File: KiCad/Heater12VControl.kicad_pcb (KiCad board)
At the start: 2 copper layers, 19.2 x 13.9 mm, 11 parts, among them J1 12V, J2 Arduino, J3 Heater, J4 Temp sensor, Q1 SI2308, Q2 IRLR3715

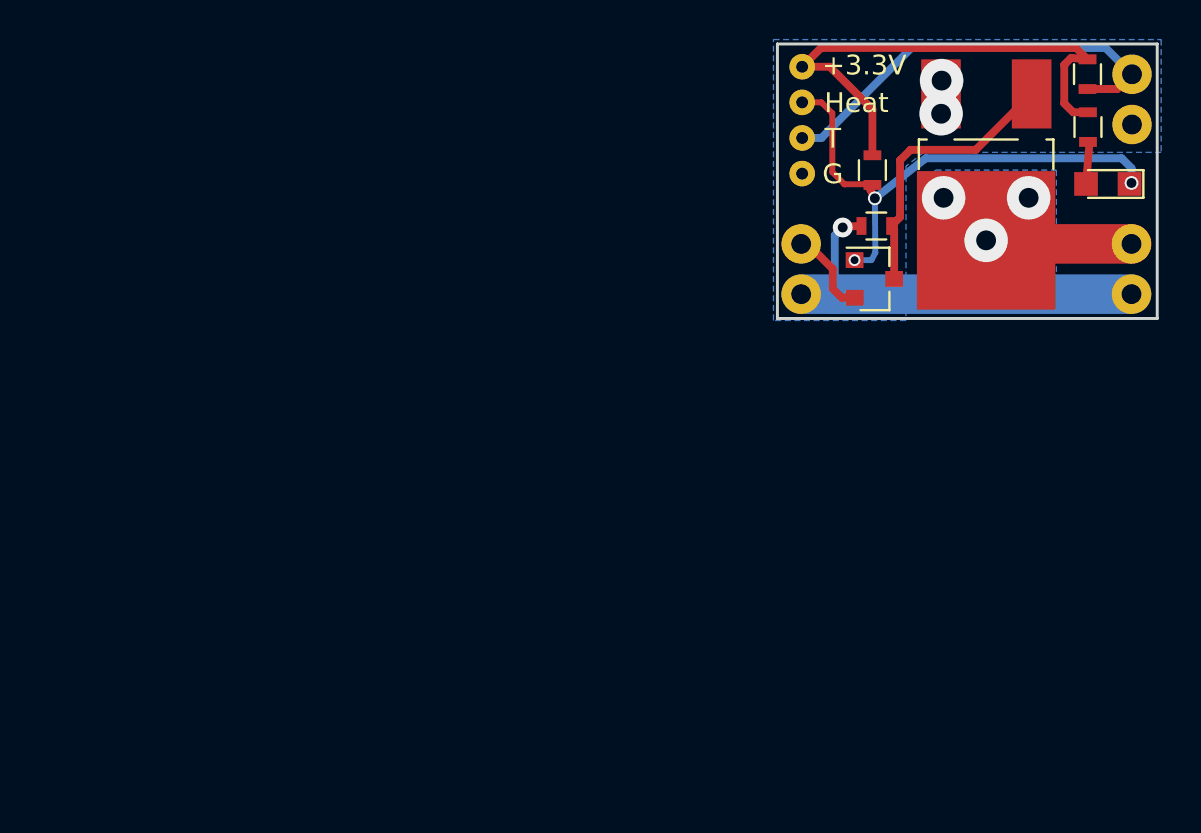
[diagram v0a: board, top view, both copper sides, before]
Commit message: New Version with rotary encoder and AIO pcb
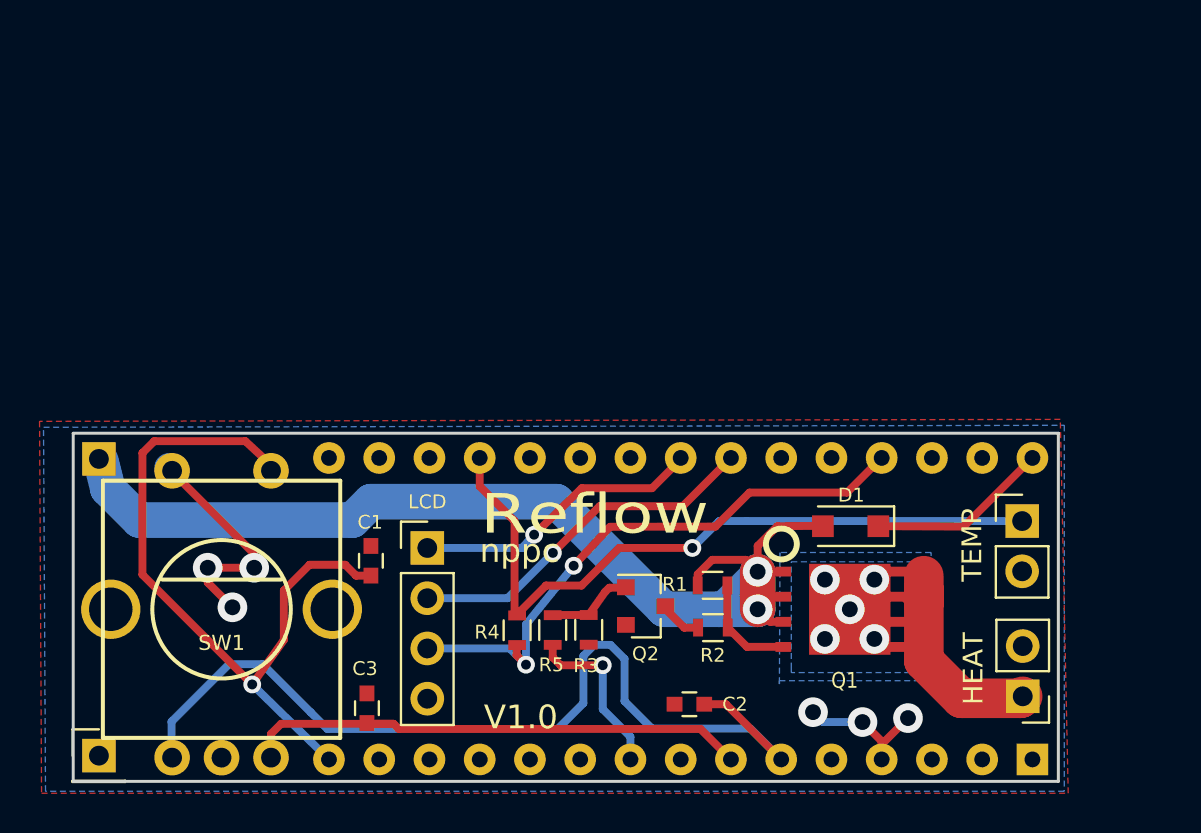
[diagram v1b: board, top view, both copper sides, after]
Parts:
- removed J1: 12V, KiCad_custom:Conn2pin_2.54mm
- removed J2: Arduino, KiCad_custom:conn_4pin_TH_1.8mm
- removed J3: Heater, KiCad_custom:Conn2pin_2.54mm
- added 12V: PWR, Pin_Headers:Pin_Header_Straight_1x01_Pitch2.54mm, F.Cu at (124.6, 119.8)
- added C1: 22n, Capacitors_SMD:C_0603, F.Cu at (138.3, 125.0)
- added C2: 22n, Capacitors_SMD:C_0603, F.Cu at (154.4, 132.2)
- added C3: 22n, Capacitors_SMD:C_0603, F.Cu at (138.2, 132.4)
- added GND: PWR, Pin_Headers:Pin_Header_Straight_1x01_Pitch2.54mm, F.Cu at (124.6, 134.8)
- added HEAT: Heater, Pin_Headers:Pin_Header_Straight_1x02_Pitch2.54mm, F.Cu at (171.3, 131.8)
- added LCD: LCD, Pin_Headers:Pin_Header_Straight_1x04_Pitch2.54mm, F.Cu at (141.2, 124.3)
- added R5: 100, Resistors_SMD:R_0603, F.Cu at (147.5, 128.4)
- added SW1: Rotary_Encoder, ROTARY-ENCODER, F.Cu at (130.8, 127.4)
- added TEMP: Temp sensor, Pin_Headers:Pin_Header_Straight_1x02_Pitch2.54mm, F.Cu at (171.3, 122.9)
- D1: value LED -> D; footprint LEDs:LED_0805 -> Diodes_SMD:D_SOD-123F
- J4: value Temp sensor -> Arduino_Nano_Header; footprint KiCad_custom:Conn2pin_2.54mm -> Modules:Arduino_Nano; moved to B.Cu
- Q1: value SI2308 -> AON6403; footprint TO_SOT_Packages_SMD:SOT-23 -> KiCadCustomLibs:DFN-8-1EP_6x5mm
- Q2: value IRLR3715 -> SI2308; footprint TO_SOT_Packages_SMD:TO-252-2_Rectifier -> TO_SOT_Packages_SMD:SOT-23
- R1: value 300 -> 100K
- R2: value 4.7K -> 1K
- R3: value 2K -> 10K
- moved R4 40.3 mm to (145.7, 128.5), turned to 270 degrees
- moved J4 33.7 mm to (171.8, 135.0), turned to 90 degrees
- moved R1 29.9 mm to (155.6, 126.2), turned to 0 degrees
- moved Q2 27.4 mm to (152.2, 127.2), turned to 0 degrees
- moved R3 25.1 mm to (149.4, 128.4), turned to 270 degrees
- moved R2 24.5 mm to (155.6, 128.3), turned to 180 degrees
- moved D1 21.6 mm to (162.6, 123.2)
- moved Q1 16.8 mm to (162.1, 127.4)
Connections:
- D1 pad 2: Net-(D1-Pad2) -> +12V
- J4 pad 1: Net-(J2-Pad2) -> Net-(J4-Pad1)
- J4 pad 2: GND -> Net-(J4-Pad2)
- Q1 pad 1: Net-(D1-Pad1) -> Net-(Q1-Pad1)
- Q1 pad 2: GND -> Net-(HEAT1-Pad1)
- Q1 pad 3: Net-(Q1-Pad3) -> +12V
- Q2 pad 1: Net-(Q1-Pad3) -> Net-(Q2-Pad1)
- Q2 pad 2: Net-(J3-Pad2) -> GND
- Q2 pad 3: GND -> Net-(Q2-Pad3)
- R1 pad 1: Net-(D1-Pad2) -> +12V
- R1 pad 2: +3V3 -> Net-(Q1-Pad1)
- R2 pad 1: Net-(D1-Pad1) -> Net-(Q1-Pad1)
- R2 pad 2: +3V3 -> Net-(Q2-Pad3)
- R3 pad 1: Net-(J1-Pad2) -> Net-(Q2-Pad1)
- R3 pad 2: Net-(Q1-Pad3) -> GND
- R4 pad 1: Net-(J2-Pad2) -> /Temp
- R4 pad 2: +3V3 -> VCC
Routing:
- net +12V: track 0.00 -> 58.9 mm, vias 0 -> 2
- net Net-(C2-Pad1): track 0.00 -> 47.0 mm
- net Net-(HEAT1-Pad1): track 0.00 -> 44.8 mm, vias 0 -> 5
- net Net-(C1-Pad1): track 0.00 -> 37.5 mm, vias 0 -> 1
- net /Temp: track 0.00 -> 36.3 mm, vias 0 -> 1
- net VCC: track 0.00 -> 30.2 mm, vias 0 -> 2
- net Net-(C3-Pad1): track 0.00 -> 26.8 mm
- net +3V3: track 26.5 -> 0.00 mm
- net Net-(J2-Pad2): track 21.7 -> 0.00 mm
- net Net-(J1-Pad2): track 21.2 -> 0.00 mm, vias 1 -> 0
- net Net-(J4-Pad24): track 0.00 -> 18.3 mm, vias 0 -> 1
- net Net-(D1-Pad1): track 26.6 -> 9.23 mm, vias 3 -> 0
- net Net-(J3-Pad2): track 16.4 -> 0.00 mm, vias 3 -> 0
- net Net-(J4-Pad23): track 0.00 -> 14.7 mm, vias 0 -> 1
- net Net-(Q1-Pad3): track 14.4 -> 0.00 mm
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- added copper zone on F.Cu, net GND
- added copper zone on B.Cu, net Net-(HEAT1-Pad1)
- removed copper zone on B.Cu, net Net-(J3-Pad2)
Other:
- board size 19.2 x 13.9 mm -> 49.8 x 17.6 mm
- net class 12V: clearance 0.4 -> 0.3; trace_width 2 -> 1.8; via_dia 2.2 -> 1.5; via_drill 1 -> 0.8
- net class Default: via_dia 0.7 -> 0.9
- net class Thin: via_dia 0.6 -> 0.7
- board text added: "Reflow"
- board text added: "V1.0"
- board text added: "nppc"
- board text removed: "+3.3V"
- board text removed: "12V"
- board text removed: "G"
- board text removed: "GND"
- board text removed: "HEAT"
- board text removed: "Heat"
- board text removed: "T"
- board text removed: "TEMP"
